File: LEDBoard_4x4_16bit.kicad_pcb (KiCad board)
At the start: 2 copper layers, 40 x 40 mm, 35 parts, among them J1 signal_in, J2 power, J6 signal_out, U1 TLC5971RGER, U2 TLC5971RGER, U3 TLC5971RGER, U4 TLC5971RGER

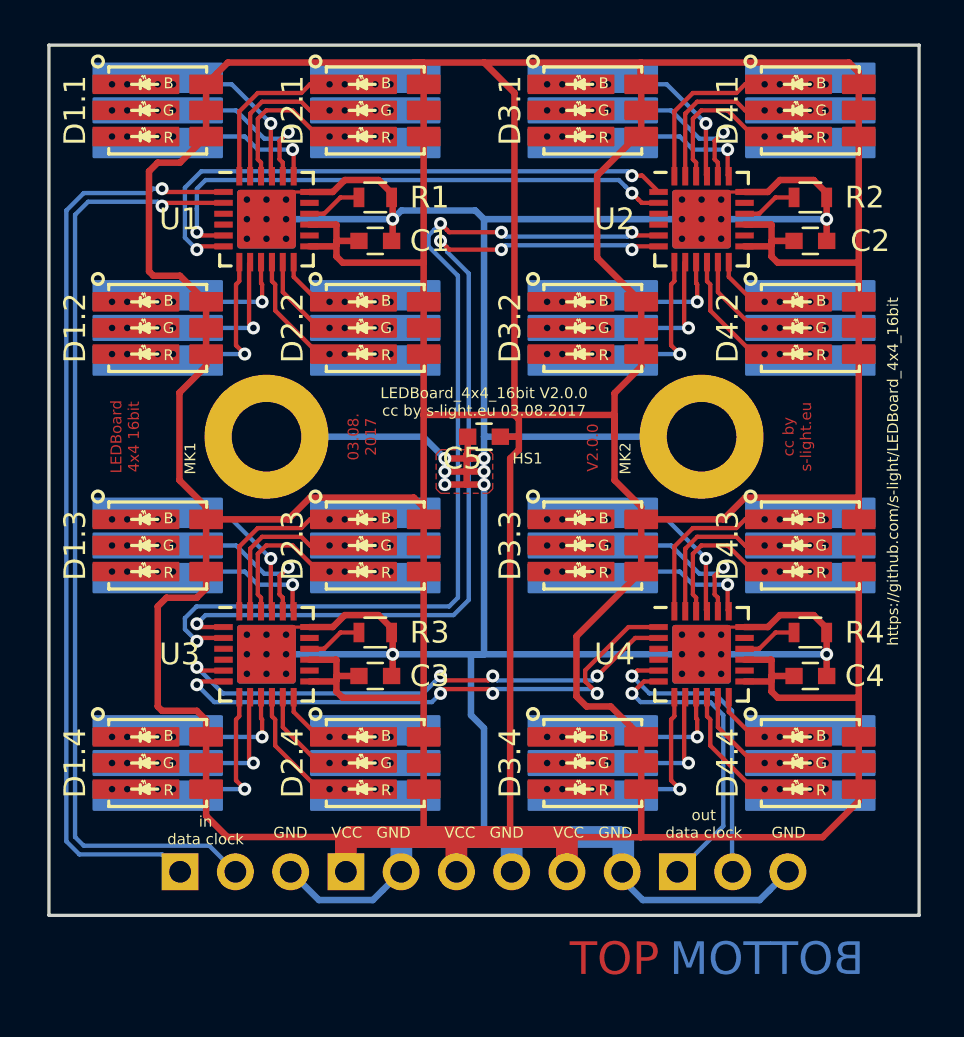
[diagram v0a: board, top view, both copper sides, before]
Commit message: pcb: changed size and corners. size: to allow for 0,5mm tolerance corners: minimal radius 0,5mm
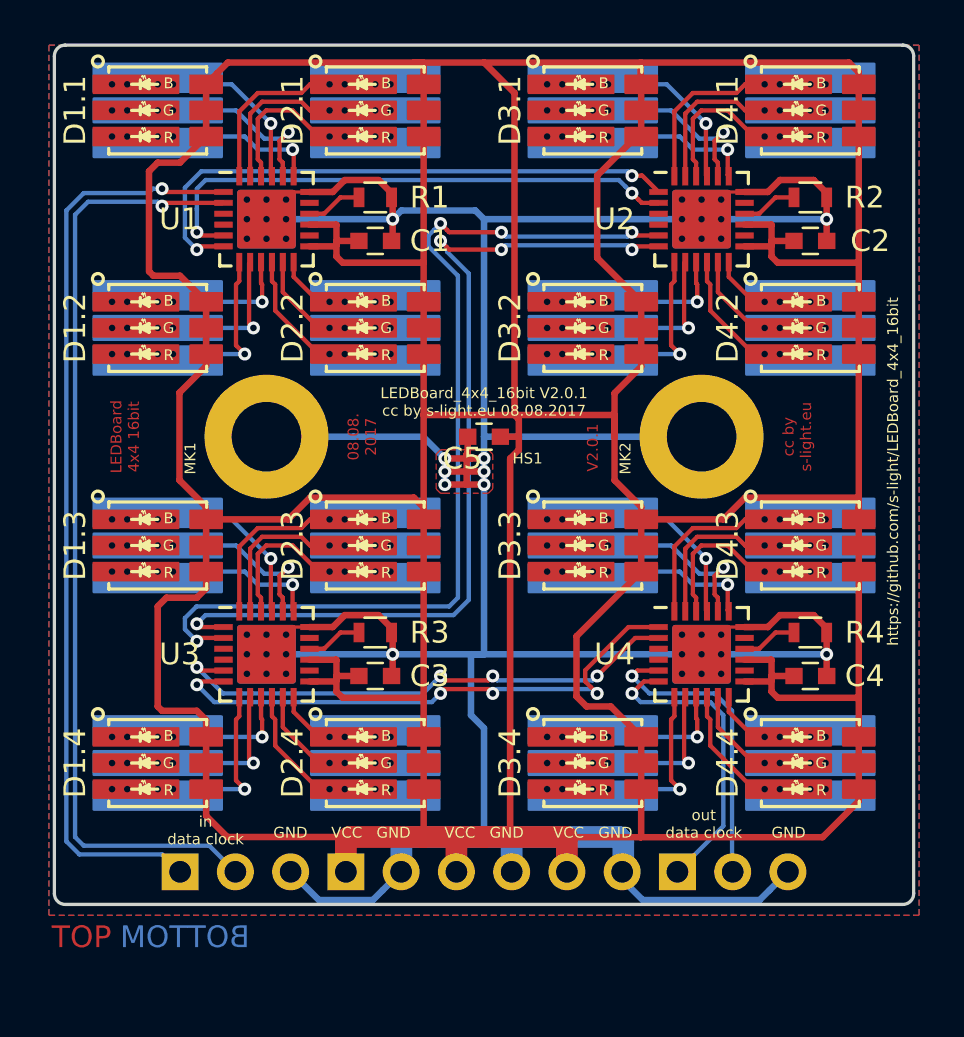
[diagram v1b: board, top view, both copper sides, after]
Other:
- board size 40 x 40 mm -> 39.5 x 39.5 mm
- board text added: "08.08. 2017"
- board text added: "LEDBoard_4x4_16bit V2.0.1 cc by s-light.eu 08.08.2017"
- board text added: "V2.0.1"
- board text removed: "03.08. 2017"
- board text removed: "LEDBoard_4x4_16bit V2.0.0 cc by s-light.eu 03.08.2017"
- board text removed: "V2.0.0"
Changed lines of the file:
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@@
-(kicad_pcb (version 20170123) (host pcbnew no-vcs-found-1f6854f~59~ubuntu17.04.1)
+(kicad_pcb (version 20170123) (host pcbnew no-vcs-found-b8c621a~59~ubuntu17.04.1)
   (general
     (thickness 1.6)
-    (drawings 45)
+    (drawings 49)
     (tracks 750)
     (zones 0)
@@
   (title_block
     (title "LEDBoard 4x4 16bit")
-    (date 03.08.2017)
-    (rev 2.0.0)
+    (date 08.08.2017)
+    (rev 2.0.1)
     (company s-light.eu)
     (comment 1 "designed by Stefan Krüger")
@@
     )
   )
-  (gr_text V2.0.0 (at 75 68.5 90) (layer F.Cu)
+  (gr_arc (start 89.25 89) (end 89.25 89.5) (angle -90) (layer Edge.Cuts) (width 0.15))
+  (gr_arc (start 89.25 50.5) (end 89.75 50.5) (angle -90) (layer Edge.Cuts) (width 0.15))
+  (gr_arc (start 50.75 50.5) (end 50.75 50) (angle -90) (layer Edge.Cuts) (width 0.15))
+  (gr_arc (start 50.75 89) (end 50.25 89) (angle -90) (layer Edge.Cuts) (width 0.15))
+  (gr_text V2.0.1 (at 75 68.5 90) (layer F.Cu)
     (effects (font (size 0.5 0.5) (thickness 0.1)))
   )
@@
     (effects (font (size 0.5 0.5) (thickness 0.1)))
   )
-  (gr_text "03.08.\n2017" (at 64.4 68 90) (layer F.Cu)
+  (gr_text "08.08.\n2017" (at 64.4 68 90) (layer F.Cu)
     (effects (font (size 0.5 0.5) (thickness 0.1)))
   )
@@
     (effects (font (size 0.5 0.5) (thickness 0.1)))
   )
-  (gr_text "LEDBoard_4x4_16bit V2.0.0\ncc by s-light.eu 03.08.2017" (at 70 66.4) (layer F.SilkS)
+  (gr_text "LEDBoard_4x4_16bit V2.0.1\ncc by s-light.eu 08.08.2017" (at 70 66.4) (layer F.SilkS)
     (effects (font (size 0.5 0.5) (thickness 0.1)))
   )
@@
   (gr_line (start 89.7 50.3) (end 89.7 89.7) (layer Dwgs.User) (width 0.05))
   (gr_line (start 50.3 50.3) (end 89.7 50.3) (layer Dwgs.User) (width 0.05))
-  (gr_line (start 50 90) (end 50 50) (layer Edge.Cuts) (width 0.15))
-  (gr_line (start 90 90) (end 50 90) (layer Edge.Cuts) (width 0.15))
-  (gr_line (start 90 50) (end 90 90) (layer Edge.Cuts) (width 0.15))
-  (gr_line (start 50 50) (end 90 50) (layer Edge.Cuts) (width 0.15))
-  (gr_text BOTTOM (at 83 92) (layer B.Cu)
-    (effects (font (size 1.5 1.5) (thickness 0.15)) (justify mirror))
+  (gr_line (start 50.25 89) (end 50.25 50.5) (layer Edge.Cuts) (width 0.15))
+  (gr_line (start 89.25 89.5) (end 50.75 89.5) (layer Edge.Cuts) (width 0.15))
+  (gr_line (start 89.75 50.5) (end 89.75 89) (layer Edge.Cuts) (width 0.15))
+  (gr_line (start 50.75 50) (end 89.25 50) (layer Edge.Cuts) (width 0.15))
+  (gr_text BOTTOM (at 56.25 91) (layer B.Cu)
+    (effects (font (size 1 1) (thickness 0.15)) (justify mirror))
   )
-  (gr_text TOP (at 76 92) (layer F.Cu)
-    (effects (font (size 1.5 1.5) (thickness 0.15)))
+  (gr_text TOP (at 51.5 91) (layer F.Cu)
+    (effects (font (size 1 1) (thickness 0.15)))
   )
   (segment (start 71.6 68.6) (end 71.6 68) (width 0.3) (layer F.Cu) (net 1))

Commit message: updated pcb to LED-Type NSSM124D
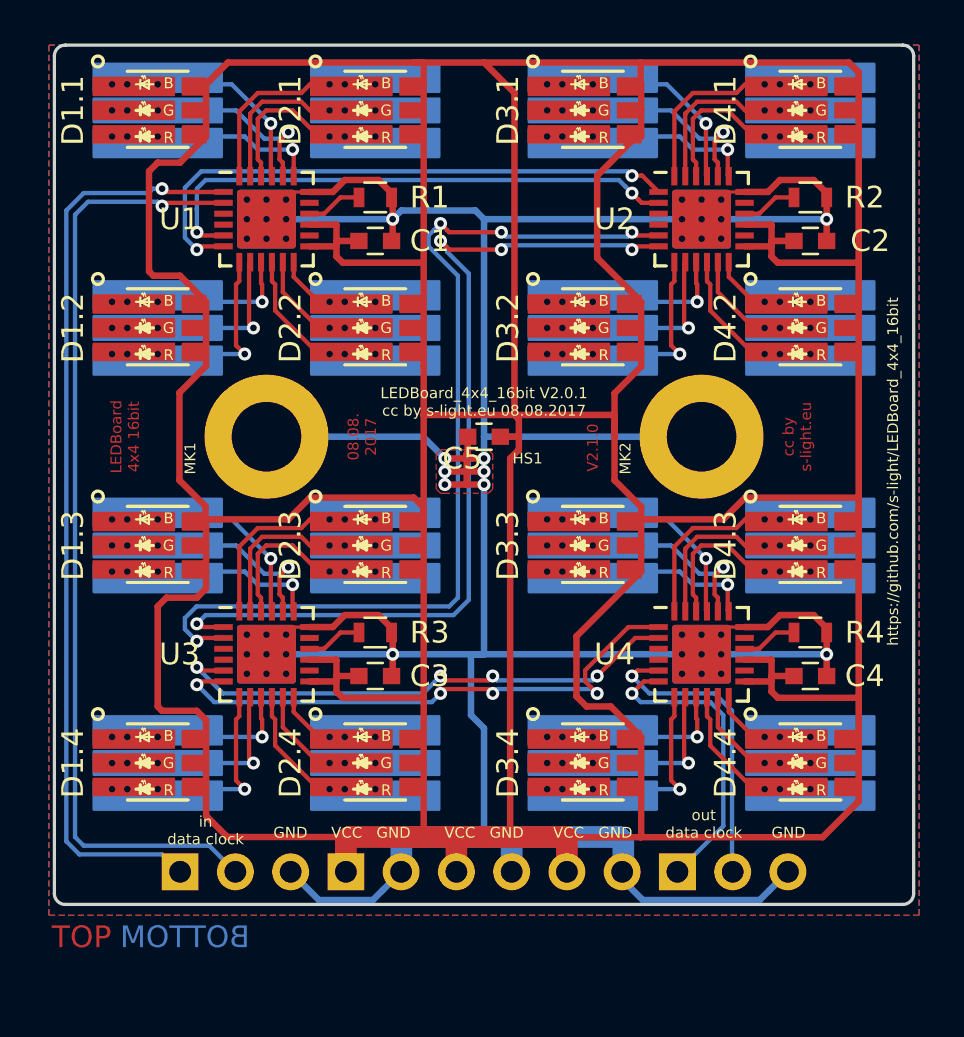
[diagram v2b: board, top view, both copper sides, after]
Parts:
- D1.1, D1.2, D1.3, D1.4, D2.1, D2.2, D2.3, D2.4, D3.1, D3.2, D3.3, D3.4, D4.1, D4.2, D4.3, D4.4: footprint nichia:LED_NSSM032AT_wViaHeatSinkBig -> nichia:LED_NSSM124_wViaHeatSinkBig_LayoutCompatibleWithNSSM032AT
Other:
- net class Default: clearance 0.15 -> 0
- rule trace_clearance: 0.15 -> 0
- board text added: "V2.1.0"
- board text removed: "V2.0.1"

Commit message: pcb updated renderings
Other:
- board text added: "LEDBoard_4x4_16bit V2.1.0 cc by s-light.eu 08.08.2017"
- board text removed: "LEDBoard_4x4_16bit V2.0.1 cc by s-light.eu 08.08.2017"
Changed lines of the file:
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@@
     (effects (font (size 0.5 0.5) (thickness 0.1)))
   )
-  (gr_text "LEDBoard_4x4_16bit V2.0.1\ncc by s-light.eu 08.08.2017" (at 70 66.4) (layer F.SilkS)
+  (gr_text "LEDBoard_4x4_16bit V2.1.0\ncc by s-light.eu 08.08.2017" (at 70 66.4) (layer F.SilkS)
     (effects (font (size 0.5 0.5) (thickness 0.1)))
   )
